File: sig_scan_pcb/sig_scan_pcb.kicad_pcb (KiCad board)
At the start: 2 copper layers, 0 parts

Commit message: Updating PCB to final design and updating partlist
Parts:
- added AE1: Antenna_Shield, RF_Antenna:Texas_SWRA117D_2.4GHz_Left, F.Cu at (115.9, 26.6)
- added C1: 1uF, Capacitor_SMD:C_0805_2012Metric, F.Cu at (30.8, 31.6)
- added C10: 100nF, Capacitor_SMD:C_0805_2012Metric, F.Cu at (40.7, 45.0)
- added C11: 22uF, Capacitor_SMD:C_0805_2012Metric, F.Cu at (72.3, 25.2)
- added C12: 100nF, Capacitor_SMD:C_0805_2012Metric, F.Cu at (32.2, 35.8)
- added C13: DNP, Capacitor_SMD:C_0805_2012Metric, F.Cu at (135.7, 42.6)
- added C14: 132nF, Capacitor_SMD:C_0805_2012Metric, F.Cu at (28.8, 37.0)
- added C15: 22uF, Capacitor_SMD:C_0805_2012Metric, F.Cu at (66.5, 27.2)
- added C16: 47uF, Capacitor_SMD:C_1206_3216Metric, F.Cu at (69.9, 24.6)
- added C17: DNP, Capacitor_SMD:C_0805_2012Metric, F.Cu at (139.6, 42.7)
- added C18: 1uF, Capacitor_SMD:C_0805_2012Metric, F.Cu at (30.6, 40.2)
- added C19: 212nF, Capacitor_SMD:C_0805_2012Metric, F.Cu at (24.3, 43.6)
- added C2: 100nF, Capacitor_SMD:C_0805_2012Metric, F.Cu at (44.5, 31.6)
- added C20: 100nF, Capacitor_SMD:C_0805_2012Metric, F.Cu at (30.6, 42.4)
- added C21: 27pF, Capacitor_SMD:C_0805_2012Metric, F.Cu at (38.5, 45.0)
- added C22: 132nF, Capacitor_SMD:C_0805_2012Metric, F.Cu at (24.4, 48.6)
- added C23: 10pF, Capacitor_SMD:C_0805_2012Metric, F.Cu at (102.6, 40.3)
- added C24: 1uF, Capacitor_SMD:C_0805_2012Metric, F.Cu at (108.5, 30.8)
- added C25: 100nF, Capacitor_SMD:C_0805_2012Metric, F.Cu at (41.3, 50.7)
- added C26: 100nF, Capacitor_SMD:C_0805_2012Metric, F.Cu at (40.3, 23.5)
- added C27: 10pF, Capacitor_SMD:C_0805_2012Metric, F.Cu at (121.2, 32.6)
- added C28: 10pF, Capacitor_SMD:C_0805_2012Metric, F.Cu at (128.9, 32.7)
- added C29: 39pF, Capacitor_SMD:C_0805_2012Metric, F.Cu at (30.8, 67.9)
- added C3: 10nF, Capacitor_SMD:C_0805_2012Metric, F.Cu at (38.6, 31.7)
- added C30: 39pF, Capacitor_SMD:C_0805_2012Metric, F.Cu at (30.8, 71.8)
- added C31: 100nF, Capacitor_SMD:C_0805_2012Metric, F.Cu at (34.7, 64.4)
- added C32: 100nF, Capacitor_SMD:C_0805_2012Metric, F.Cu at (47.1, 48.9)
- added C33: 2.2uF, Capacitor_SMD:C_0805_2012Metric, F.Cu at (38.6, 60.1)
- added C34: 10uF, Capacitor_SMD:C_0805_2012Metric, F.Cu at (32.2, 79.0)
- added C35: 100nF, Capacitor_SMD:C_0805_2012Metric, F.Cu at (44.9, 49.0)
- added C36: 100nF, Capacitor_SMD:C_0805_2012Metric, F.Cu at (33.9, 67.6)
- added C37: 100nF, Capacitor_SMD:C_0805_2012Metric, F.Cu at (35.9, 55.6)
- added C38: 100nF, Capacitor_SMD:C_0805_2012Metric, F.Cu at (38.6, 62.1)
- added C39: 100nF, Capacitor_SMD:C_0805_2012Metric, F.Cu at (35.9, 53.6)
- added C4: 330pF, Capacitor_SMD:C_0805_2012Metric, F.Cu at (48.0, 34.4)
- added C40: 1uF, Capacitor_SMD:C_0805_2012Metric, F.Cu at (119.6, 36.6)
- added C41: 10nF, Capacitor_SMD:C_0805_2012Metric, F.Cu at (119.6, 38.6)
- added C42: 10uF, Capacitor_SMD:C_0805_2012Metric, F.Cu at (110.3, 36.9)
- added C43: 1uF, Capacitor_SMD:C_0805_2012Metric, F.Cu at (111.2, 38.9)
- added C44: 100nF, Capacitor_SMD:C_0805_2012Metric, F.Cu at (112.8, 41.0)
- added C45: 100nF, Capacitor_SMD:C_0805_2012Metric, F.Cu at (116.8, 44.1)
- added C46: 100nF, Capacitor_SMD:C_0805_2012Metric, F.Cu at (121.0, 51.6)
- added C47: 1uF, Capacitor_SMD:C_0805_2012Metric, F.Cu at (129.3, 45.8)
- added C48: 100nF, Capacitor_SMD:C_0805_2012Metric, F.Cu at (129.3, 47.9)
- added C49: 100nF, Capacitor_SMD:C_0805_2012Metric, F.Cu at (127.7, 39.6)
- added C5: 100nF, Capacitor_SMD:C_0805_2012Metric, F.Cu at (46.6, 31.6)
- added C50: 10uF, Capacitor_SMD:C_0805_2012Metric, F.Cu at (62.4, 73.2)
- added C51: 100nF, Capacitor_SMD:C_0805_2012Metric, F.Cu at (63.3, 76.1)
- added C52: 10nF, Capacitor_SMD:C_0805_2012Metric, F.Cu at (61.2, 76.1)
- added C53: 1.5pF, Capacitor_SMD:C_0805_2012Metric, F.Cu at (115.0, 36.6)
- added C54: 1.5pF, Capacitor_SMD:C_0805_2012Metric, F.Cu at (114.9, 30.7)
- added C55: 100nF, Capacitor_SMD:C_0805_2012Metric, F.Cu at (48.3, 67.5)
- added C56: 100nF, Capacitor_SMD:C_0805_2012Metric, F.Cu at (37.1, 76.1)
- added C57: 100nF, Capacitor_SMD:C_0805_2012Metric, F.Cu at (48.3, 69.5)
- added C58: 1.5pF, Capacitor_SMD:C_0805_2012Metric, F.Cu at (111.3, 28.1)
- added C59: 10uF, Capacitor_SMD:C_0805_2012Metric, F.Cu at (37.1, 78.2)
- added C6: 6n8F, Capacitor_SMD:C_0805_2012Metric, F.Cu at (50.9, 35.5)
- added C60: 100nF, Capacitor_SMD:C_0805_2012Metric, F.Cu at (48.3, 71.6)
- added C61: 100nF, Capacitor_SMD:C_0805_2012Metric, F.Cu at (47.2, 74.5)
- added C62: 2.2uF, Capacitor_SMD:C_0805_2012Metric, F.Cu at (49.2, 74.5)
- added C63: 22pF, Capacitor_SMD:C_0805_2012Metric, F.Cu at (94.6, 59.5)
- added C64: 1uF, Capacitor_SMD:C_0805_2012Metric, F.Cu at (91.4, 60.0)
- added C65: 100nF, Capacitor_SMD:C_0805_2012Metric, F.Cu at (134.4, 68.1)
- added C66: 10uF, Capacitor_SMD:C_0805_2012Metric, F.Cu at (135.0, 75.5)
- added C67: 1uF, Capacitor_SMD:C_0805_2012Metric, F.Cu at (86.0, 51.0)
- added C68: 100nF, Capacitor_SMD:C_0805_2012Metric, F.Cu at (133.0, 75.5)
- added C69: 100nF, Capacitor_SMD:C_0805_2012Metric, F.Cu at (86.8, 65.8)
- added C7: 10uF, Capacitor_SMD:C_0805_2012Metric, F.Cu at (66.5, 23.5)
- added C70: 1uF, Capacitor_SMD:C_0805_2012Metric, F.Cu at (82.2, 59.6)
- added C71: 100nF, Capacitor_SMD:C_0805_2012Metric, F.Cu at (80.8, 56.0)
- added C72: 100nF, Capacitor_SMD:C_0805_2012Metric, F.Cu at (78.8, 56.0)
- added C73: 10uF, Capacitor_SMD:C_0805_2012Metric, F.Cu at (74.8, 71.6)
- added C74: 1uF, Capacitor_SMD:C_0805_2012Metric, F.Cu at (74.7, 69.5)
- added C75: 10uF, Capacitor_SMD:C_0805_2012Metric, F.Cu at (68.7, 59.8)
- added C76: 22pF, Capacitor_SMD:C_0805_2012Metric, F.Cu at (77.8, 51.9)
- added C77: 100nF, Capacitor_SMD:C_0805_2012Metric, F.Cu at (75.7, 51.9)
- added C78: 1uF, Capacitor_SMD:C_0805_2012Metric, F.Cu at (67.7, 39.6)
- added C8: 10uF, Capacitor_SMD:C_0805_2012Metric, F.Cu at (72.4, 29.1)
- added C9: 100nF, Capacitor_SMD:C_0805_2012Metric, F.Cu at (48.0, 38.4)
- added D1: 1N4007FL, Diode_SMD:D_SOD-123, F.Cu at (138.4, 54.1)
- added D2: 1N4007FL, Diode_SMD:D_SOD-123, F.Cu at (147.3, 46.6)
- added D3: VSSAF5M6HM3/H, Diode_SMD:D_SMA, F.Cu at (92.4, 67.1)
- added D4: 7012X5, LED_SMD:LED_0805_2012Metric, F.Cu at (95.3, 56.7)
- added D5: 7012X5, LED_SMD:LED_0805_2012Metric, F.Cu at (88.4, 54.1)
- added D6: VSSAF5M6HM3/H, Diode_SMD:D_SMA, F.Cu at (77.5, 59.7)
- added D7: 1N4007FL, Diode_SMD:D_SOD-123, F.Cu at (68.0, 35.3)
- added FB1: Bead, Capacitor_SMD:C_0805_2012Metric, F.Cu at (38.3, 58.1)
- added FB2: Bead, Capacitor_SMD:C_0805_2012Metric, F.Cu at (39.8, 77.2)
- added IC1: AZ1117H-3.3TRE1, AZ1117H-3_3TRE1:SOT230P700X180-4N, F.Cu at (78.1, 26.1)
- added IC2: BQ24650RVAR, BQ24650RVAR:QFN50P350X350X100-17N-D, F.Cu at (86.1, 58.3)
- added J1: CON-SMA-EDGE-S, CON_SMA_EDGE_S:RFSOLUTIONS_CON-SMA-EDGE-S, F.Cu at (23.8, 32.6)
- added J10: PROG, Connector_PinHeader_2.54mm:PinHeader_1x04_P2.54mm_Vertical, F.Cu at (133.5, 28.7)
- added J11: Solar connector, TB007_508_02BE:CUI_TB007-508-02BE, F.Cu at (145.3, 64.8)
- added J12: TS Conn, Connector_PinHeader_2.54mm:PinHeader_1x03_P2.54mm_Vertical, F.Cu at (100.9, 55.7)
- added J13: Conn_01x03_Pin, Jumper:SolderJumper-3_P1.3mm_Bridged12_RoundedPad1.0x1.5mm, F.Cu at (83.6, 50.7)
- added J14: BAT connector, TB007_508_02BE:CUI_TB007-508-02BE, F.Cu at (63.2, 34.9)
- added J2: 12V Connector, TB007_508_02BE:CUI_TB007-508-02BE, F.Cu at (145.3, 54.5)
- added J4: UJ20-C-H-G-SMT-P16-TR, Connector_USB:USB_C_Receptacle_G-Switch_GT-USB-7010ASV, F.Cu at (148.5, 36.0)
- added J5: USB Switch, Connector_PinHeader_2.54mm:PinHeader_1x03_P2.54mm_Vertical, F.Cu at (143.9, 43.6)
- added J6: LED Connector, Connector_PinHeader_2.54mm:PinHeader_1x02_P2.54mm_Vertical, F.Cu at (75.6, 37.5)
- added J7: CLK TP, Connector_PinHeader_2.54mm:PinHeader_1x01_P2.54mm_Vertical, F.Cu at (30.2, 62.7)
- added J8: Conn, Connector_PinHeader_2.54mm:PinHeader_1x04_P2.54mm_Vertical, F.Cu at (32.2, 58.1)
- added J9: LED Connector, Connector_PinHeader_2.54mm:PinHeader_1x02_P2.54mm_Vertical, F.Cu at (135.3, 46.8)
- added JP1: SolderJumper_2_Open, Jumper:SolderJumper-2_P1.3mm_Open_RoundedPad1.0x1.5mm, F.Cu at (27.7, 31.0)
- added JP2: SP, Jumper:SolderJumper-3_P1.3mm_Bridged12_RoundedPad1.0x1.5mm, F.Cu at (136.0, 33.3)
- added JP3: SP, Jumper:SolderJumper-3_P1.3mm_Bridged12_RoundedPad1.0x1.5mm, F.Cu at (132.4, 31.8)
- added JP4: SolderJumper_2_Open, Jumper:SolderJumper-2_P1.3mm_Open_RoundedPad1.0x1.5mm, F.Cu at (92.4, 72.1)
- added JP5: SolderJumper_2_Open, Jumper:SolderJumper-2_P1.3mm_Open_RoundedPad1.0x1.5mm, F.Cu at (76.0, 47.1)
- added L1: 100nH, Inductor_SMD:L_0805_2012Metric, F.Cu at (32.3, 27.9)
- added L10: 24nH, Inductor_SMD:L_0805_2012Metric, F.Cu at (122.3, 37.5)
- added L11: 10uH, Inductor_SMD:L_0805_2012Metric, F.Cu at (32.3, 77.1)
- added L12: 2nH, Inductor_SMD:L_0603_1608Metric, F.Cu at (114.0, 43.2)
- added L13: 2.7nH, Inductor_SMD:L_0805_2012Metric, F.Cu at (115.9, 33.7)
- added L14: 2.7nH, Inductor_SMD:L_0805_2012Metric, F.Cu at (114.8, 28.1)
- added L15: PIS150H-471M, PIS150H-471M:PIS150H471M, F.Cu at (103.2, 70.6)
- added L16: 10uH, IHLP2525CZER100M01:IND_IHLP_2525_CZ_VIS, F.Cu at (68.4, 67.4)
- added L17: PIS150H-471M, PIS150H-471M:PIS150H471M, F.Cu at (65.1, 49.7)
- added L2: 8n2H, Inductor_SMD:L_0805_2012Metric, F.Cu at (36.5, 33.6)
- added L3: 150nH, Inductor_SMD:L_0805_2012Metric, F.Cu at (41.6, 32.5)
- added L4: 150nH, Inductor_SMD:L_0805_2012Metric, F.Cu at (41.6, 30.8)
- added L5: 118.1nH, Inductor_SMD:L_0603_1608Metric, F.Cu at (31.4, 37.9)
- added L6: 478nH, Inductor_SMD:L_0603_1608Metric, F.Cu at (25.3, 41.0)
- added L7: 470uH, SRR1260-471K:SRR12604R7Y, F.Cu at (85.3, 37.7)
- added L8: 478nH, Inductor_SMD:L_0603_1608Metric, F.Cu at (25.3, 46.1)
- added L9: 118.1nH, Inductor_SMD:L_0603_1608Metric, F.Cu at (25.3, 51.1)
- added Q1: AO3407A, Package_TO_SOT_SMD:SOT-23, F.Cu at (37.2, 23.5)
- added Q2: AO3407A, Package_TO_SOT_SMD:SOT-23, F.Cu at (134.4, 71.5)
- added Q3: SI7540DP-T1-GE3, SI7288DP-T1-GE3:TRANS_SI7540DP-T1-GE3, F.Cu at (77.5, 65.5)
- added R1: 1K8, Resistor_SMD:R_0805_2012Metric, F.Cu at (48.0, 36.4)
- added R10: 22, Resistor_SMD:R_0805_2012Metric, F.Cu at (31.3, 45.1)
- added R11: 1K, Resistor_SMD:R_0805_2012Metric, F.Cu at (51.4, 40.4)
- added R12: 100K, Resistor_SMD:R_0805_2012Metric, F.Cu at (42.3, 23.5)
- added R13: 220, Resistor_SMD:R_0805_2012Metric, F.Cu at (75.6, 34.3)
- added R14: 220, Resistor_SMD:R_0805_2012Metric, F.Cu at (41.3, 26.3)
- added R15: 10K, Resistor_SMD:R_0805_2012Metric, F.Cu at (108.4, 34.8)
- added R16: 10K, Resistor_SMD:R_0805_2012Metric, F.Cu at (108.4, 32.8)
- added R17: 4K7, Resistor_SMD:R_0805_2012Metric, F.Cu at (28.1, 68.9)
- added R18: 100, Resistor_SMD:R_0805_2012Metric, F.Cu at (41.3, 47.8)
- added R19: 4K7, Resistor_SMD:R_0805_2012Metric, F.Cu at (118.0, 52.9)
- added R2: 10K, Resistor_SMD:R_0805_2012Metric, F.Cu at (48.0, 40.4)
- added R20: 4K7, Resistor_SMD:R_0805_2012Metric, F.Cu at (28.0, 70.9)
- added R21: 4K7, Resistor_SMD:R_0805_2012Metric, F.Cu at (116.1, 52.9)
- added R22: 10K, Resistor_SMD:R_0805_2012Metric, F.Cu at (143.3, 47.2)
- added R23: 6K8, Resistor_SMD:R_0805_2012Metric, F.Cu at (141.4, 47.2)
- added R24: 0 Ohm, Resistor_SMD:R_0805_2012Metric, F.Cu at (32.2, 75.3)
- added R25: 499, Resistor_SMD:R_0805_2012Metric, F.Cu at (133.2, 38.9)
- added R26: 220, Resistor_SMD:R_0805_2012Metric, F.Cu at (132.5, 46.8)
- added R27: 4K7, Resistor_SMD:R_0805_2012Metric, F.Cu at (133.3, 34.8)
- added R28: 10K, Resistor_SMD:R_0805_2012Metric, F.Cu at (48.3, 65.4)
- added R29: 4K7, Resistor_SMD:R_0805_2012Metric, F.Cu at (131.3, 34.8)
- added R3: 5K1, Resistor_SMD:R_0805_2012Metric, F.Cu at (141.8, 39.6)
- added R30: 10K, Resistor_SMD:R_0805_2012Metric, F.Cu at (98.0, 50.5)
- added R31: 499K, Resistor_SMD:R_0805_2012Metric, F.Cu at (96.7, 59.5)
- added R32: 36K, Resistor_SMD:R_0805_2012Metric, F.Cu at (99.5, 58.6)
- added R33: 5K23, Resistor_SMD:R_0805_2012Metric, F.Cu at (94.1, 54.1)
- added R34: 30K1, Resistor_SMD:R_0805_2012Metric, F.Cu at (91.2, 51.3)
- added R35: 10K, Resistor_SMD:R_0805_2012Metric, F.Cu at (98.0, 55.8)
- added R36: 10, Resistor_SMD:R_0805_2012Metric, F.Cu at (91.4, 62.0)
- added R37: 100, Resistor_SMD:R_0805_2012Metric, F.Cu at (91.2, 54.8)
- added R38: 100K, Resistor_SMD:R_0805_2012Metric, F.Cu at (134.4, 66.1)
- added R39: 220, Resistor_SMD:R_0805_2012Metric, F.Cu at (137.1, 67.1)
- added R4: 0, Resistor_SMD:R_0805_2012Metric, F.Cu at (138.6, 39.9)
- added R40: 10K, Resistor_SMD:R_0805_2012Metric, F.Cu at (89.2, 51.3)
- added R41: 2.2, Resistor_SMD:R_0805_2012Metric, F.Cu at (87.8, 63.1)
- added R42: 0.033, Resistor_SMD:R_1206_3216Metric, F.Cu at (68.9, 62.3)
- added R43: 499K, Resistor_SMD:R_0805_2012Metric, F.Cu at (79.9, 51.9)
- added R44: 100K, Resistor_SMD:R_0805_2012Metric, F.Cu at (79.9, 48.5)
- added R5: 0, Resistor_SMD:R_0805_2012Metric, F.Cu at (136.6, 39.9)
- added R6: 5K1, Resistor_SMD:R_0805_2012Metric, F.Cu at (141.9, 32.4)
- added R7: 22, Resistor_SMD:R_0805_2012Metric, F.Cu at (33.2, 45.1)
- added R8: 22, Resistor_SMD:R_0805_2012Metric, F.Cu at (47.0, 45.5)
- added R9: 22, Resistor_SMD:R_0805_2012Metric, F.Cu at (44.9, 45.5)
- added SW1: BOOT, Button_Switch_SMD:SW_Tactile_SPST_NO_Straight_CK_PTS636Sx25SMTRLFS, F.Cu at (99.7, 37.0)
- added SW2: RESET, Button_Switch_SMD:SW_Tactile_SPST_NO_Straight_CK_PTS636Sx25SMTRLFS, F.Cu at (99.7, 29.8)
- added T1: TCM1-382WX+, TCM1-382WX+:TCM1382WX, F.Cu at (27.0, 55.5)
- added U1: BAV99-7-F, BAV99-7-F:SOT-23_DIO, F.Cu at (34.3, 30.7)
- added U2: AZ1117H-5.0TRE1, AZ1117H-5.0TRE1:SOT230P700X180-4N, F.Cu at (60.7, 25.4)
- added U3: R820T, R820T:QFN50P400X400X90-25N, F.Cu at (39.1, 38.2)
- added U4: ESP32-S3FN8, Package_DFN_QFN:QFN-56-1EP_7x7mm_P0.4mm_EP4x4mm, F.Cu at (123.3, 45.3)
- added U5: RTL2832U, RTL2832U:QFN40P600X600X100-49N, F.Cu at (40.0, 69.7)
- added U6: M24C02-WMN, Package_SO:SOIC-8_3.9x4.9mm_P1.27mm, F.Cu at (57.3, 72.6)
- added U7: RA-02_LORA, RA-02_LORA:MODULE_RA-02_LORA, F.Cu at (122.3, 71.5)
- added Y1: 28.8MHz, ATX-11-F-32.000MHZ-F05-T:ATX11F32000MHZF05T, F.Cu at (37.1, 49.6)
- added Y2: 40MHz, ABM8-40.000MHZ-10-B1U-T:ABM810000MHZ12D2W, F.Cu at (125.1, 32.7)
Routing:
- net +5V: track 0.00 -> 139.8 mm, vias 0 -> 1
- net /USBD-: track 0.00 -> 133.5 mm, vias 0 -> 2
- net /USBD+: track 0.00 -> 130.6 mm, vias 0 -> 4
- net +15V: track 0.00 -> 120.9 mm
- net /SCL: track 0.00 -> 112.5 mm, vias 0 -> 3
- net /SDA: track 0.00 -> 112.5 mm, vias 0 -> 3
- net +1V2: track 0.00 -> 102.8 mm, vias 0 -> 3
- net /GPIO1: track 0.00 -> 90.4 mm, vias 0 -> 2
- net +3.3V: track 0.00 -> 75.1 mm, vias 0 -> 10
- net GNDA: track 0.00 -> 72.7 mm, vias 0 -> 4
- net +16V: track 0.00 -> 68.5 mm
- net GND: track 0.00 -> 63.5 mm, vias 0 -> 426
- net 3.3V: track 0.00 -> 60.2 mm, vias 0 -> 13
- net Net-(IC2-SRN): track 0.00 -> 41.7 mm
- net Net-(D7-A): track 0.00 -> 41.4 mm
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- added copper zone on In2.Cu, net +3.3V
- added copper zone on In2.Cu, net 3.3V
- added copper zone on B.Cu, net GND
- added copper zone on F.Cu, net GND
- added copper zone on In1.Cu, net GND
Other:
- board outline added: 130 x 60 mm
- copper layers 2 -> 4
- board text added: "+"
- board text added: "-"
- board text added: "DC 12V"
- board text added: "DEV: SIG-SCAN"
- board text added: "OTG"
- board text added: "REV: V1.0"
- board text added: "SN: SIG-SCAN- ____________________"
- board text added: "SOLAR IN"
- board text added: "USB"

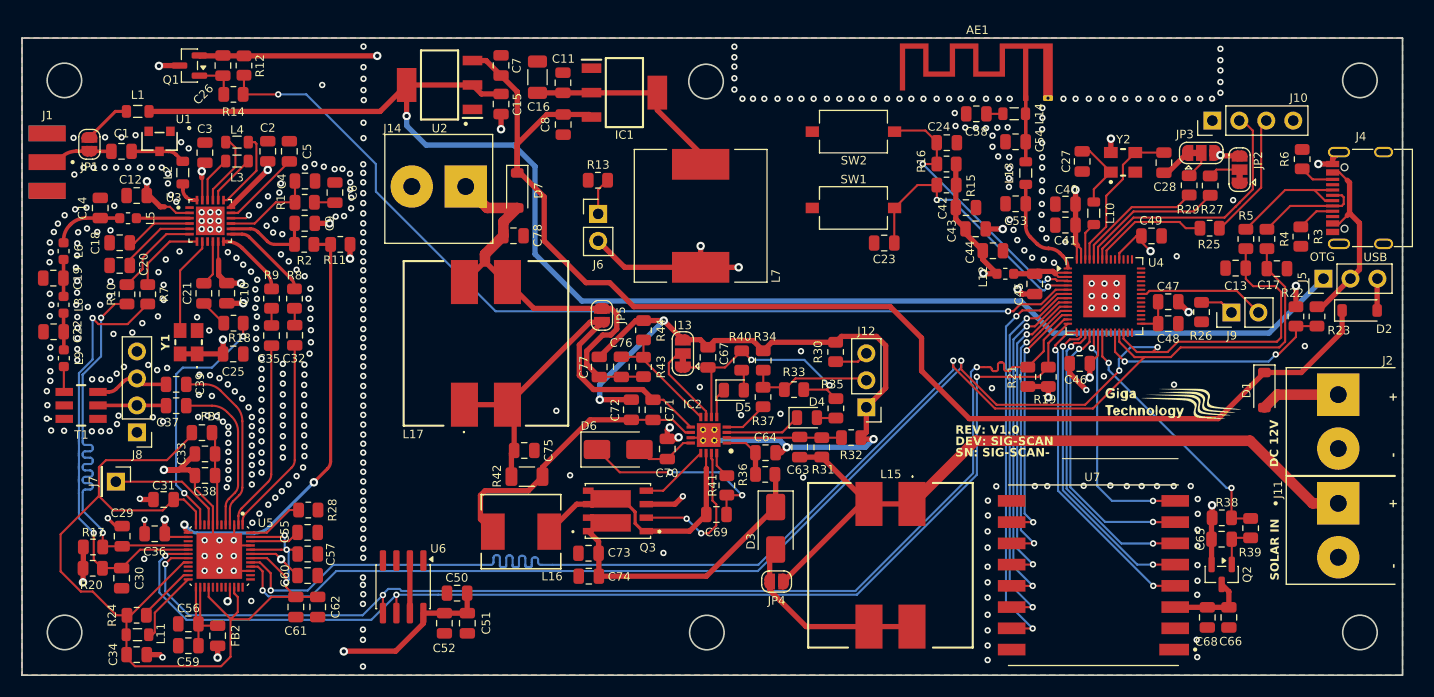
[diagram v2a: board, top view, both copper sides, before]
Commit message: Updating ground planes for solar chip and updating Gerber files
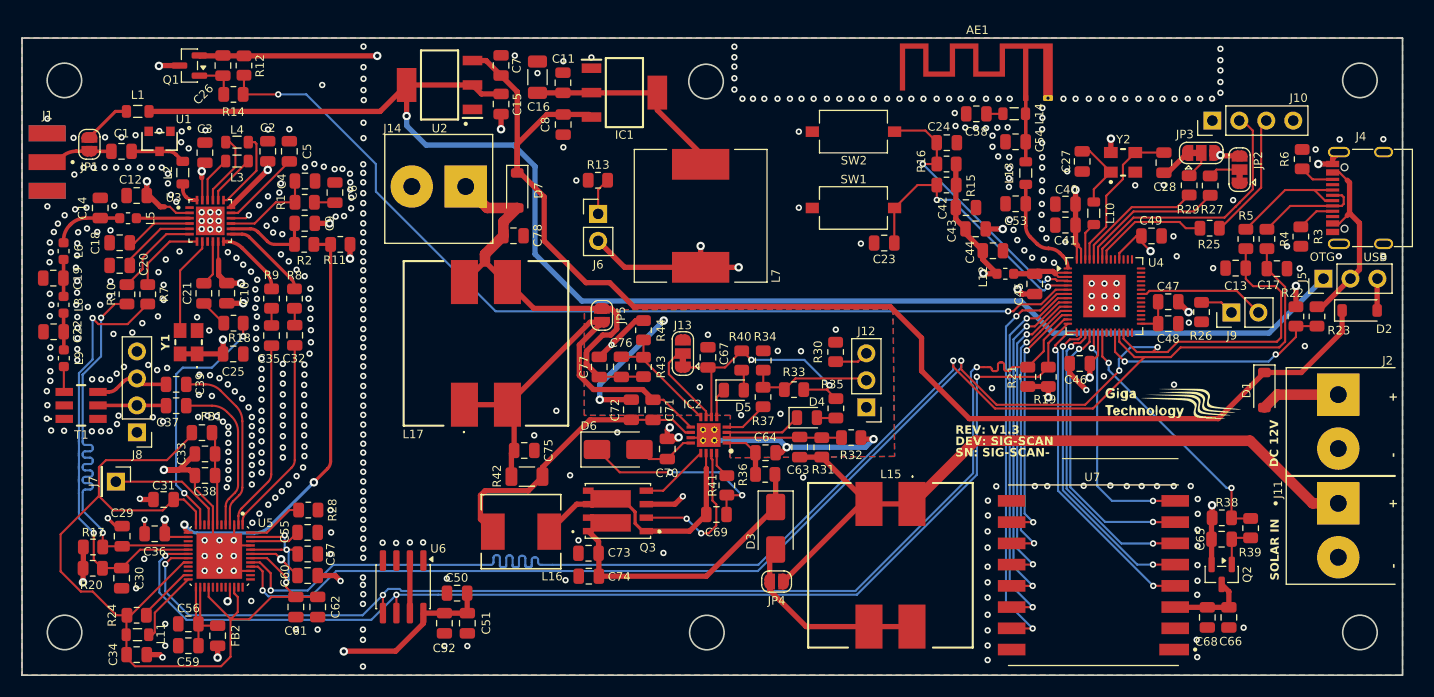
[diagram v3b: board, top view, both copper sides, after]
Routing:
- net GNDA: track 72.7 -> 37.6 mm, vias 4 -> 12
- net GND: track 63.5 -> 65.9 mm, vias 426 -> 472
- added copper zone on B.Cu, net GNDA
- added copper zone on F.Cu, net GNDA
- added copper zone on In1.Cu, net GNDA
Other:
- board text added: "REV: V1.3"
- board text removed: "REV: V1.0"
